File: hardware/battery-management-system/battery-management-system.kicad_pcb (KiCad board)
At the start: 4 copper layers, 100 x 100 mm, 146 parts, among them J1 CELLS, J10 TEMP_CELL3, J11 TEMP_CELL4, J2 Charge, J3 Discharge, J4 VBAT_DISCHARGE, J5 VBAT_CHARGE, J6 AMPHENOL_micro_usb_10118194-0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, J7 ARM-JTAG-SWD, J8 TEMP_CELL1, J9 TEMP_CELL2, Q1 DMN3404L, Q10 DMN3404L, Q11 BS250FTA, Q12 BS250FTA, Q13 BS250FTA, Q14 BS250FTA, Q15 BS250FTA, Q2 TJ40S04M3L, Q3 TJ40S04M3L, Q4 DMN3404L, Q5 DMN3404L, Q6 DMN3404L, Q7 DMN3404L, Q8 DMN3404L, Q9 DMN3404L, U1 ICL7660, U10 LM2904M8-13, U2 L6982CDR, U3 L6982CDR, U4 ICL7660, U5 FT230XS, U6 AT24C512C, U7 NCT75DR2G, U8 STM32L071CZTx, U9 LM2904M8-13

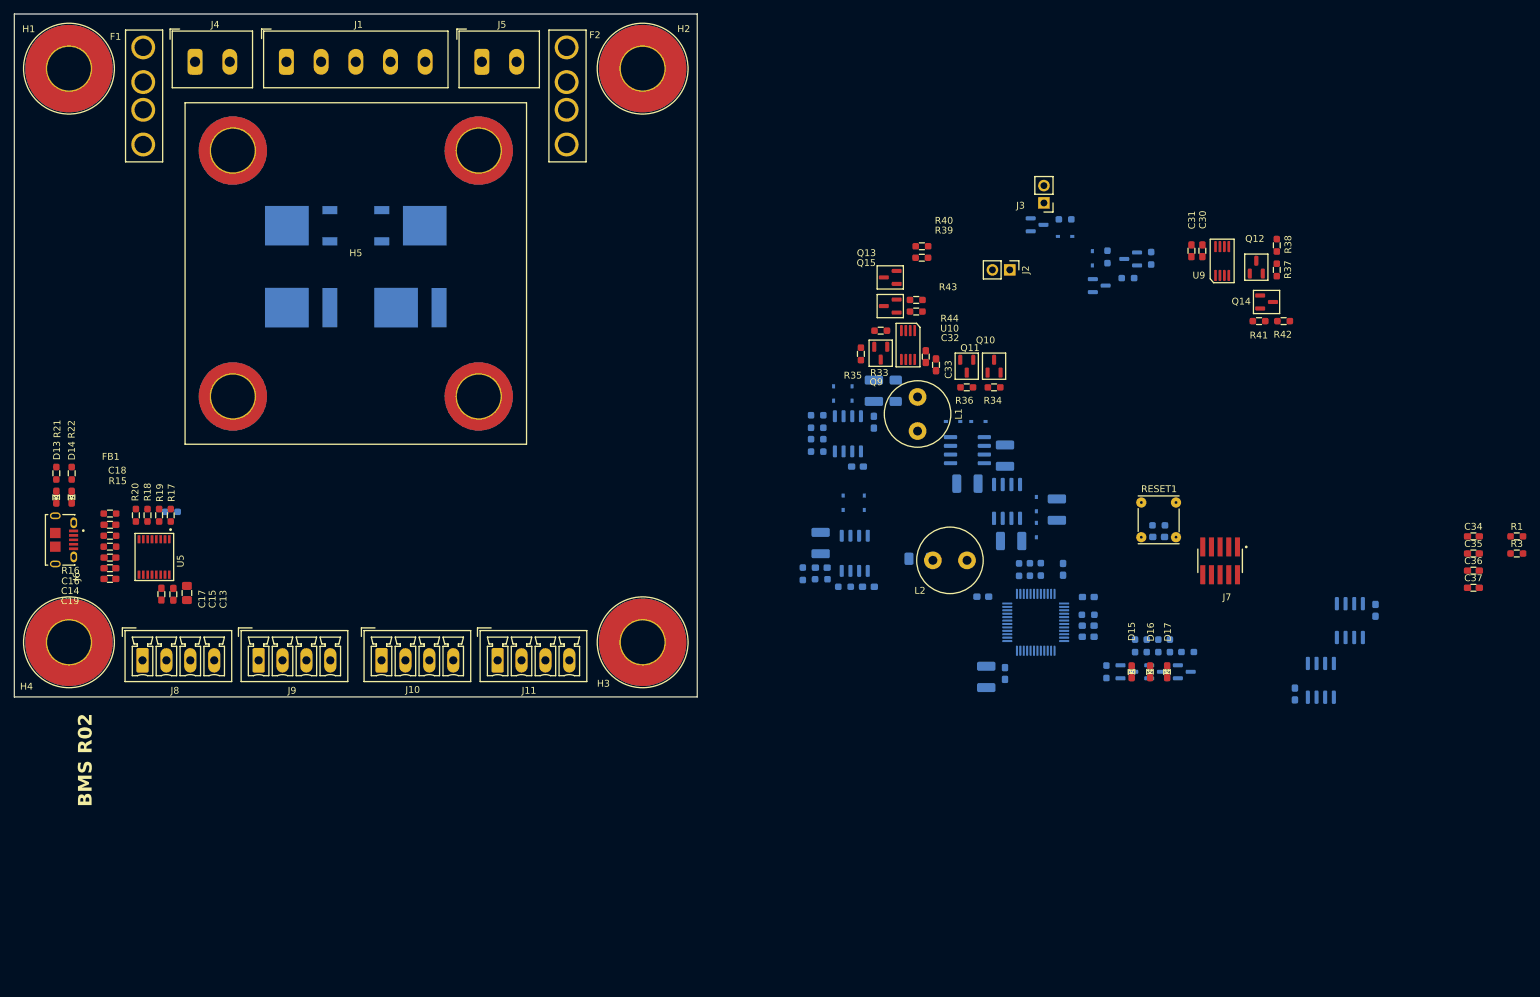
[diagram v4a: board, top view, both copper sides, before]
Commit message: layout BMS R02
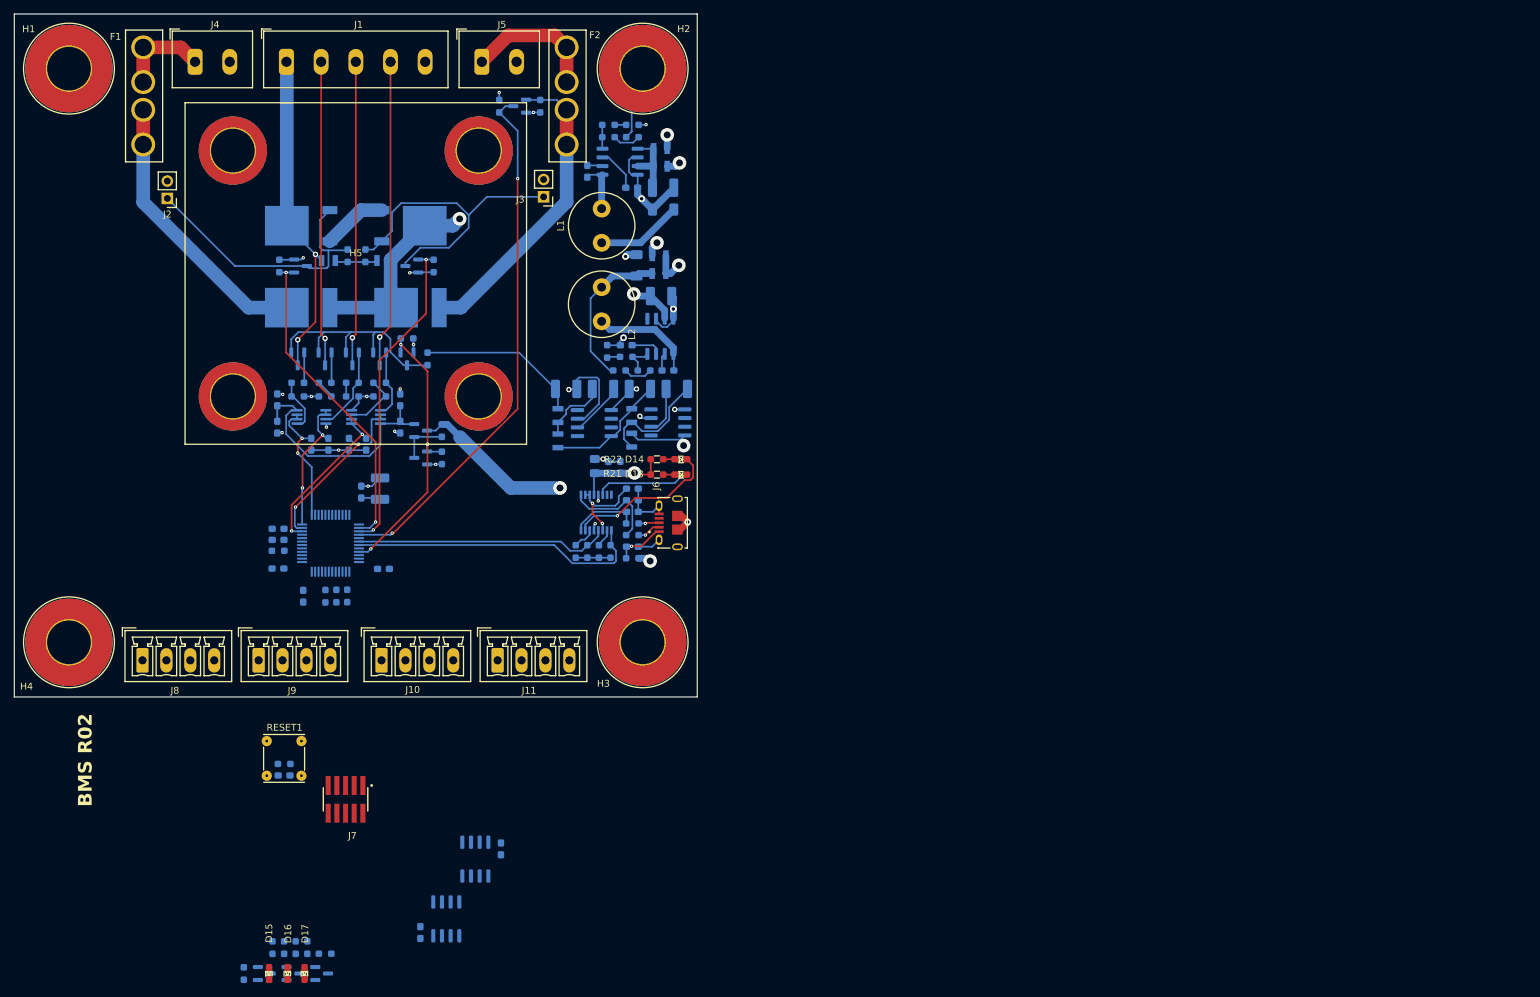
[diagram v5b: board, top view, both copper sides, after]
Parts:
- C13, C14, C15, C16, C17, C18, C19, C30, C31, C32, C33, C34, C35, C36, C37, FB1, Q10, Q11, Q12, Q13, Q14, Q15, Q9, R1, R15, R16, R17, R18, R19, R20, R3, R33, R34, R35, R36, R37, R38, R39, R40, R41, R42, R43, R44, U10, U5, U9: moved to B.Cu
- moved R1 185.5 mm to (58.8, 56.9), turned to 90 degrees
- moved C34 170.7 mm to (63.5, 83.0), turned to -90 degrees
- moved C35 168.4 mm to (66.0, 83.0), turned to -90 degrees
- moved C36 165.7 mm to (69.0, 83.0), turned to -90 degrees
- moved R3 164.1 mm to (81.4, 56.9), turned to -90 degrees
- moved C37 163.5 mm to (71.5, 83.0), turned to -90 degrees
- moved R38 145.1 mm to (61.5, 76.0), turned to 0 degrees
- moved R37 144.3 mm to (61.5, 74.0), turned to 180 degrees
- moved Q12 141.0 mm to (61.5, 70.5), turned to -90 degrees
- moved C30 137.2 mm to (58.5, 76.5), turned to 90 degrees
- moved R42 136.8 mm to (69.5, 76.0)
- moved C31 136.3 mm to (58.5, 80.5)
- moved U9 135.3 mm to (63.5, 79.0), turned to 180 degrees
- moved Q14 134.1 mm to (69.5, 70.5), turned to -90 degrees
- moved D15 133.8 mm to (57.3, 160.5)
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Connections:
- R39 pad 2: Net-(U10B-+) -> Net-(R39-Pad2)
- R40 pad 1: Net-(U10B-+) -> Net-(R39-Pad2)
- R41 pad 2: Net-(U9A-+) -> Net-(R41-Pad2)
- R42 pad 1: Net-(U9A-+) -> Net-(R41-Pad2)
- U10 pad 5: Net-(U10B-+) -> Net-(Q15-D)
- U10 pad 6: /Cell Measurement/CELL3 -> /Cell Measurement/CELL2
- U10 pad 7: /Cell Measurement/CELL3 -> /Cell Measurement/CELL2
- U9 pad 1: /Cell Measurement/CELL2 -> /Cell Measurement/CELL3
- U9 pad 2: /Cell Measurement/CELL2 -> /Cell Measurement/CELL3
- U9 pad 3: Net-(U9A-+) -> Net-(Q14-D)
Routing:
- net GND: track 0.00 -> 117.0 mm, vias 0 -> 26
- net /5V_USB: track 0.00 -> 105.0 mm, vias 0 -> 4
- net /PACK_EXT: track 0.00 -> 91.7 mm, vias 0 -> 3
- net /5V: track 0.00 -> 84.7 mm, vias 0 -> 3
- net /Battery Pack/CHARGE_AVAILABLE: track 0.00 -> 77.8 mm, vias 0 -> 2
- net /Battery Pack/PACK: track 0.00 -> 48.6 mm, vias 0 -> 2
- net /DISCHARGE: track 0.00 -> 47.3 mm, vias 0 -> 2
- net /CHARGE: track 0.00 -> 46.9 mm, vias 0 -> 2
- net Net-(J3-Pin_1): track 0.00 -> 46.1 mm
- net Net-(D4-A): track 0.00 -> 45.1 mm
- net /Battery Pack/CELL2_MINUS: track 0.00 -> 45.1 mm, vias 0 -> 1
- net /Battery Pack/CELL4_MINUS: track 0.00 -> 44.7 mm, vias 0 -> 1
- net /Battery Pack/CELL3_MINUS: track 0.00 -> 44.6 mm, vias 0 -> 1
- net /MCU/UART_USB_RX: track 0.00 -> 43.8 mm
- net /EN_CELL_MEASUREMENT: track 0.00 -> 42.2 mm, vias 0 -> 3
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- added copper zone on In1.Cu, net /3V3
- added copper zone on In2.Cu, net GND

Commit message: route BMS R02
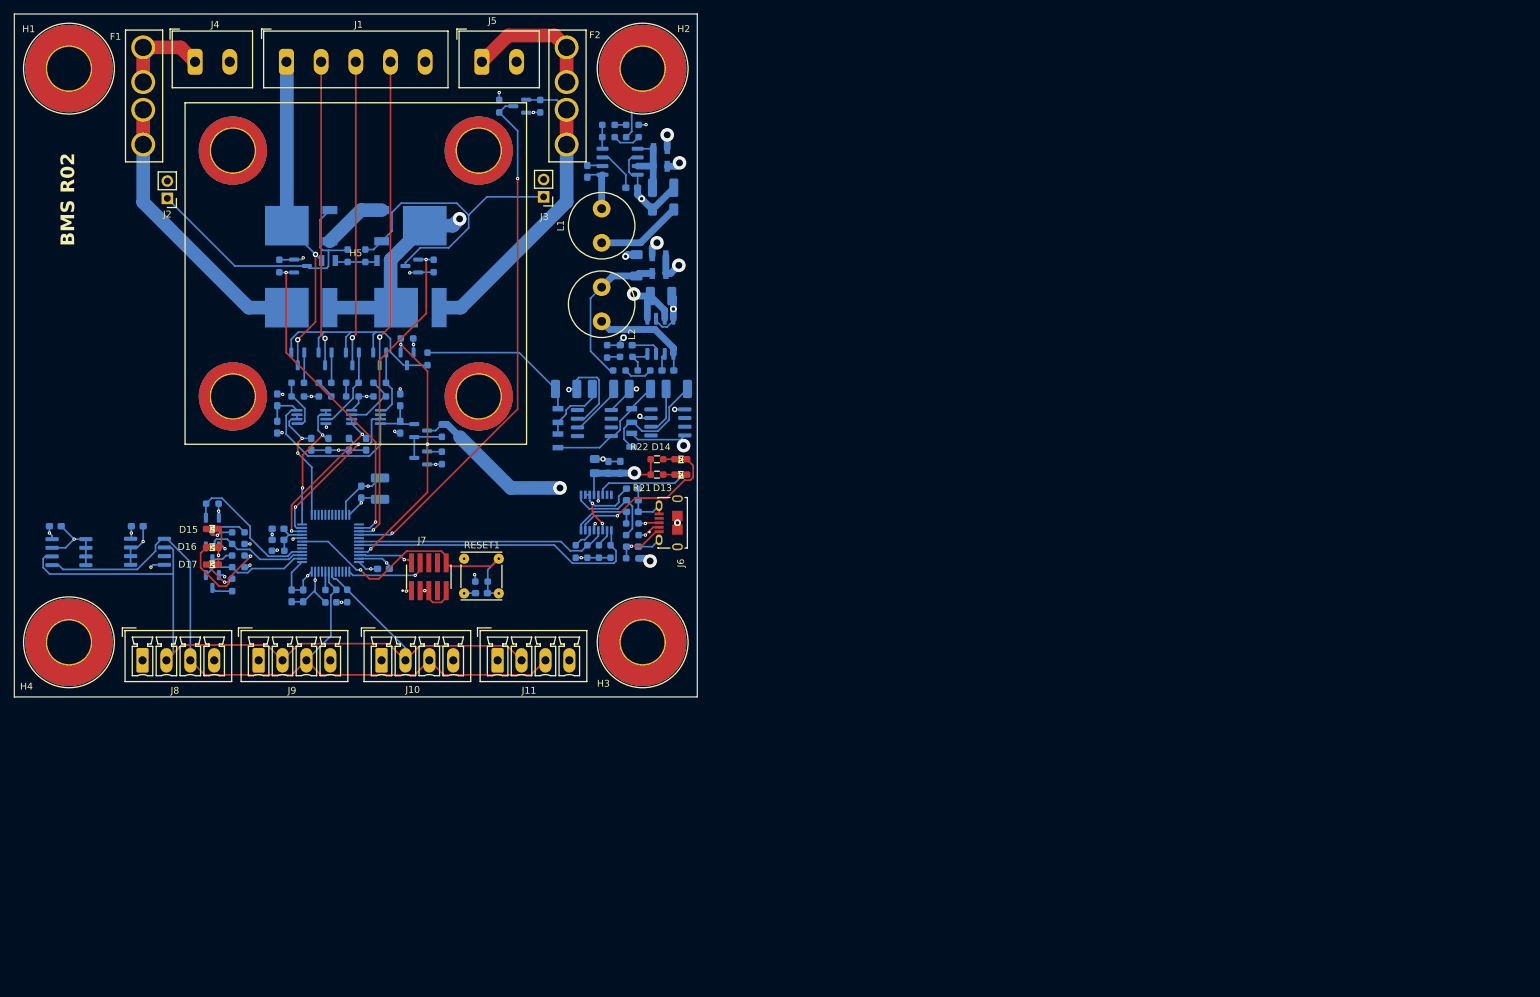
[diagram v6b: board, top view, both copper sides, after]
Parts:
- moved C20 80.0 mm to (26.0, 95.0), turned to 0 degrees
- moved U6 77.0 mm to (28.0, 98.8), turned to 180 degrees
- moved C23 71.2 mm to (38.0, 95.0), turned to 0 degrees
- moved R23 69.0 mm to (49.0, 91.7), turned to 180 degrees
- moved Q6 66.2 mm to (49.0, 94.7), turned to -90 degrees
- moved U7 65.8 mm to (39.5, 98.8), turned to 180 degrees
- moved D15 65.6 mm to (49.0, 95.4), turned to 0 degrees
- moved D16 63.4 mm to (49.0, 98.1), turned to 0 degrees
- moved Q7 62.7 mm to (49.0, 98.9), turned to -90 degrees
- moved D17 61.4 mm to (49.0, 100.6), turned to 0 degrees
- moved R24 61.0 mm to (52.8, 95.9), turned to 0 degrees
- moved Q8 59.6 mm to (49.0, 103.1), turned to -90 degrees
- moved R25 59.5 mm to (52.8, 97.6), turned to 180 degrees
- moved R26 58.0 mm to (52.8, 99.3), turned to 180 degrees
- moved R28 56.6 mm to (52.8, 101.0), turned to 180 degrees
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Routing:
- net /MCU/SCL: track 0.00 -> 115.5 mm
- net /MCU/SDA: track 0.00 -> 111.2 mm
- net GND: track 117.0 -> 173.1 mm, vias 26 -> 39
- net /MCU/NRST: track 0.00 -> 42.1 mm, vias 0 -> 1
- net /3V3: track 22.7 -> 52.5 mm, vias 2 -> 13
- net /MCU/LED1: track 0.00 -> 21.2 mm
- net /MCU/LED2: track 0.00 -> 16.2 mm
- net /MCU/LED3: track 0.00 -> 15.7 mm
- net Net-(D16-K): track 0.00 -> 15.0 mm, vias 0 -> 1
- net /MCU/SWCLK: track 0.00 -> 12.0 mm, vias 0 -> 1
- net /MCU/SWDIO: track 0.00 -> 8.15 mm, vias 0 -> 1
- net /MCU/VDDA: track 0.00 -> 5.78 mm
- net Net-(Q6-D): track 0.00 -> 5.27 mm
- net Net-(D17-K): track 0.00 -> 5.06 mm, vias 0 -> 1
- net Net-(D15-K): track 0.00 -> 4.32 mm, vias 0 -> 1
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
